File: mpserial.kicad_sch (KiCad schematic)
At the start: 12 parts, among them J1 USB_A, Q1 Q_Photo_NPN, U1 FT230XS, U2 ${SIM.PARAMS}

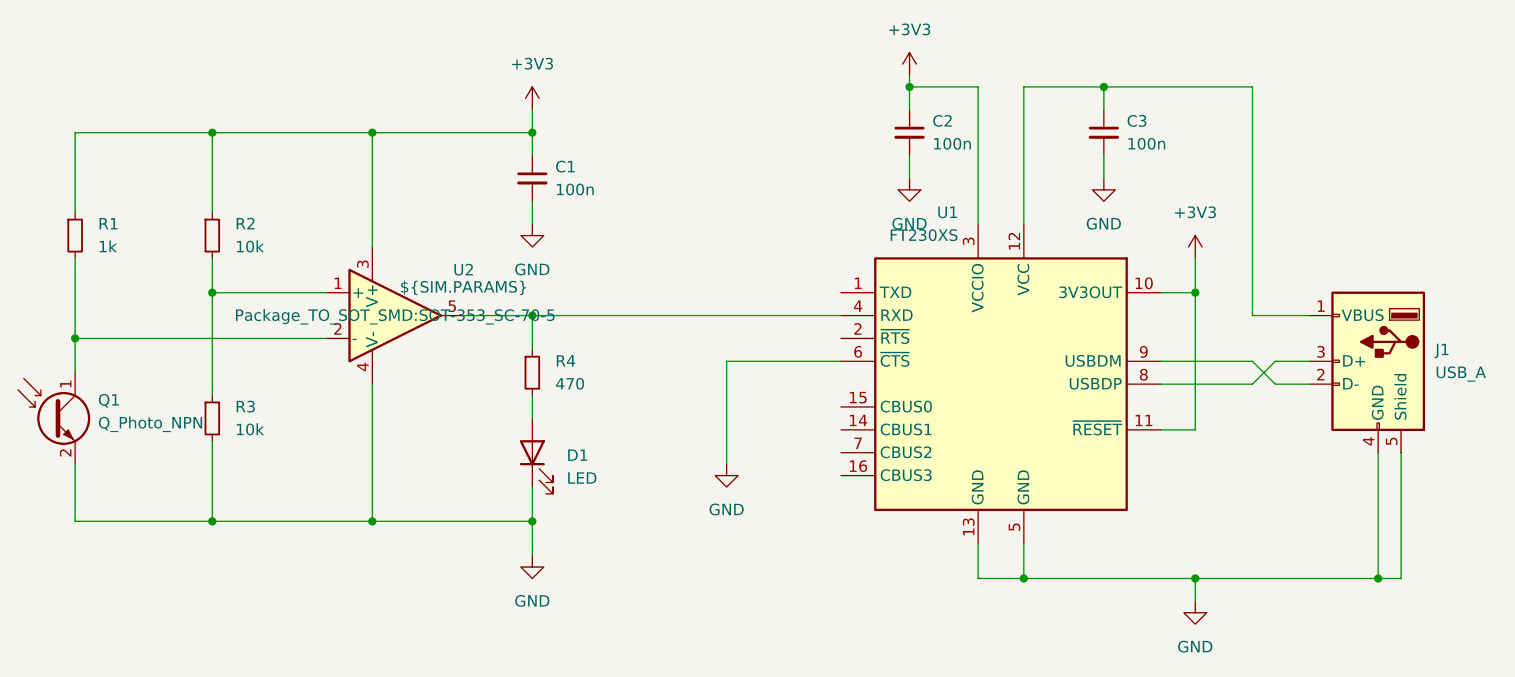
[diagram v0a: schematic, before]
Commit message: corrected opamp footprint and symbol names, changed USB-A connector to throughhole for cheaper assembly
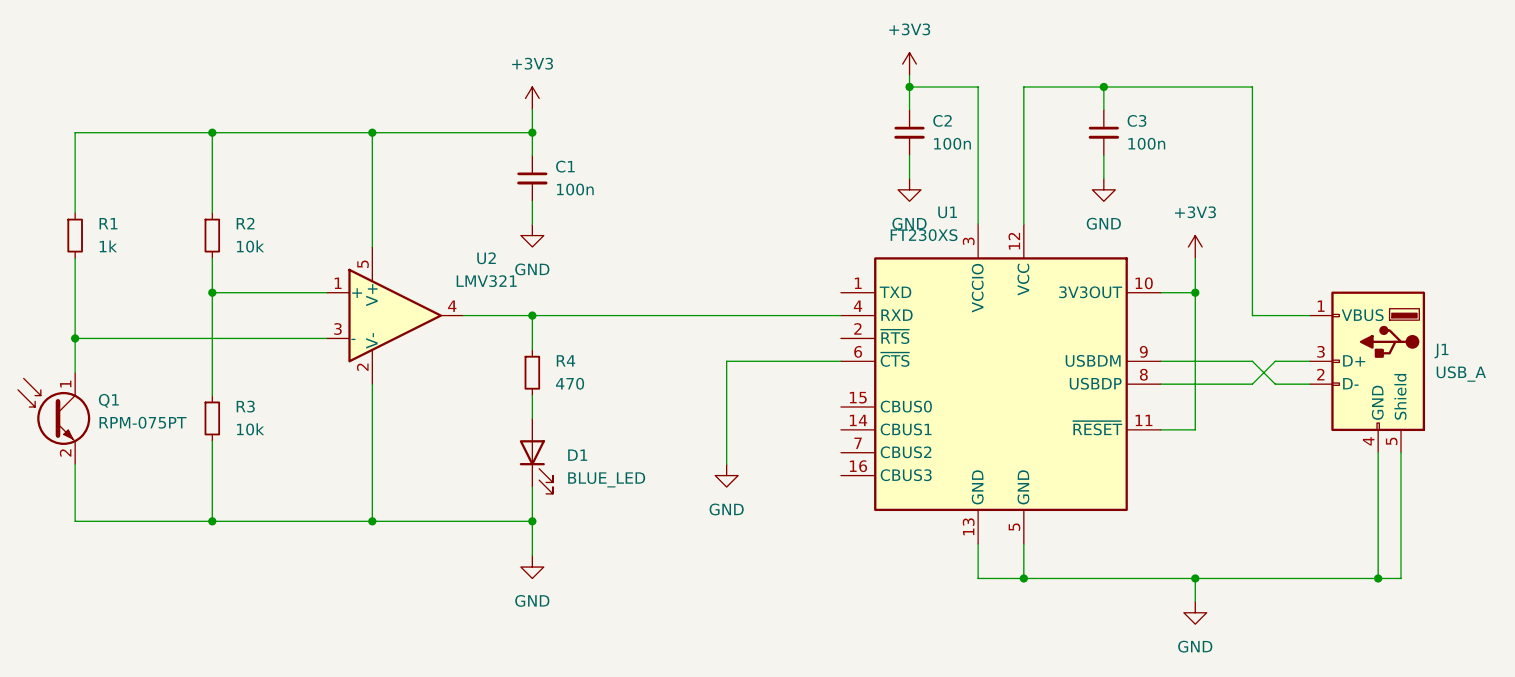
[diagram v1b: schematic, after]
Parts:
- removed U2: ${SIM.PARAMS}, Package_TO_SOT_SMD:SOT-353_SC-70-5, symbol Simulation_SPICE:OPAMP
- added U2: LMV321, Package_TO_SOT_SMD:SOT-353_SC-70-5, symbol Amplifier_Operational:LMV321
- D1: value LED -> BLUE_LED
- J1: footprint Connector_USB:USB_A_Molex_48037-2200_Horizontal -> My Footprints:CONN_USB_A_MALE_HORIZONTAL_TH
- Q1: value Q_Photo_NPN -> RPM-075PT
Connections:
- net +3V3: now also U2.5 (V+)
- net GND: now also U2.2 (V-)
- net at R4.1, U1.4 (RXD): now also U2.4
- net at R2.2, R3.1: now also U2.1 (+)
- net at Q1.1 (C), R1.2: now also U2.3 (-)
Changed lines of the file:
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@@
-	)
-	(symbol
-		(lib_id "Simulation_SPICE:OPAMP")
-		(at 74.93 87.63 0)
-		(unit 1)
-		(exclude_from_sim no)
-		(in_bom yes)
-		(on_board yes)
-		(dnp no)
-		(fields_autoplaced yes)
-		(property "Reference" "U2"
-			(at 82.55 82.5814 0)
-			(effects
-				(font
-					(size 1.27 1.27)
-				)
-			)
-		)
-		(property "Value" "${SIM.PARAMS}"
-			(at 82.55 84.4865 0)
-			(effects
-				(font
-					(size 1.27 1.27)
-				)
-			)
-		)
-		(property "Footprint" "Package_TO_SOT_SMD:SOT-353_SC-70-5"
-			(at 74.93 87.63 0)
-			(effects
-				(font
-					(size 1.27 1.27)
-				)
-			)
-		)
-		(property "Datasheet" "https://ngspice.sourceforge.io/docs/ngspice-html-manual/manual.xhtml#sec__SUBCKT_Subcircuits"
-			(at 74.93 87.63 0)
-			(effects
-				(font
-					(size 1.27 1.27)
-				)
-				(hide yes)
-			)
-		)
-		(property "Description" "Operational amplifier, single, node sequence=1:+ 2:- 3:OUT 4:V+ 5:V-"
-			(at 74.93 87.63 0)
-			(effects
-				(font
-					(size 1.27 1.27)
-				)
-				(hide yes)
-			)
-		)
-		(property "Sim.Pins" "1=in+ 2=in- 3=vcc 4=vee 5=out"
-			(at 74.93 87.63 0)
-			(effects
-				(font
-					(size 1.27 1.27)
-				)
-				(hide yes)
-			)
-		)
-		(property "Sim.Device" "SUBCKT"
-			(at 74.93 87.63 0)
-			(effects
-				(font
-					(size 1.27 1.27)
-				)
-				(justify left)
-				(hide yes)
-			)
-		)
-		(property "Sim.Library" "${KICAD8_SYMBOL_DIR}/Simulation_SPICE.sp"
-			(at 74.93 87.63 0)
-			(effects
-				(font
-					(size 1.27 1.27)
-				)
-				(hide yes)
-			)
-		)
-		(property "Sim.Name" "kicad_builtin_opamp"
-			(at 74.93 87.63 0)
-			(effects
-				(font
-					(size 1.27 1.27)
-				)
-				(hide yes)
-			)
-		)
-		(pin "1"
-		)
-		(pin "3"
-		)
-		(pin "5"
-		)
-		(pin "4"
-		)
-		(pin "2"
-		)
-		(instances
-			(project ""
-				(path "/7ebcebd8-6e74-48ea-a3c7-a4b7113dc1a4"
-					(reference "U2")
-					(unit 1)
-				)
-			)
-		)
 	)
 	(symbol
@@
 			)
 		)
-		(property "Footprint" "Connector_USB:USB_A_Molex_48037-2200_Horizontal"
+		(property "Footprint" "My Footprints:CONN_USB_A_MALE_HORIZONTAL_TH"
 			(at 180.34 93.98 0)
 			(effects
@@
 	)
 	(symbol
+		(lib_id "Amplifier_Operational:LMV321")
+		(at 74.93 87.63 0)
+		(unit 1)
+		(exclude_from_sim no)
+		(in_bom yes)
+		(on_board yes)
+		(dnp no)
+		(fields_autoplaced yes)
+		(property "Reference" "U2"
+			(at 85.09 81.3114 0)
+			(effects
+				(font
+					(size 1.27 1.27)
+				)
+			)
+		)
+		(property "Value" "LMV321"
+			(at 85.09 83.8514 0)
+			(effects
+				(font
+					(size 1.27 1.27)
+				)
+			)
+		)
+		(property "Footprint" "Package_TO_SOT_SMD:SOT-353_SC-70-5"
+			(at 74.93 87.63 0)
+			(effects
+				(font
+					(size 1.27 1.27)
+				)
+				(justify left)
+				(hide yes)
+			)
+		)
+		(property "Datasheet" "http://www.ti.com/lit/ds/symlink/lmv324.pdf"
+			(at 74.93 87.63 0)
+			(effects
+				(font
+					(size 1.27 1.27)
+				)
+				(hide yes)
+			)
+		)
+		(property "Description" "Low-Voltage Rail-to-Rail Output Operational Amplifiers, SOT-23-5/SC-70-5"
+			(at 74.93 87.63 0)
+			(effects
+				(font
+					(size 1.27 1.27)
+				)
+				(hide yes)
+			)
+		)
+		(pin "2"
+		)
+		(pin "4"
+		)
+		(pin "3"
+		)
+		(pin "5"
+		)
+		(pin "1"
+		)
+		(instances
+			(project ""
+				(path "/7ebcebd8-6e74-48ea-a3c7-a4b7113dc1a4"
+					(reference "U2")
+					(unit 1)
+				)
+			)
+		)
+	)
+	(symbol
 		(lib_id "Device:C_Small")
 		(at 132.08 67.31 0)
@@
 			)
 		)
-		(property "Value" "Q_Photo_NPN"
+		(property "Value" "RPM-075PT"
 			(at 41.91 99.5806 0)
 			(effects
@@
 			)
 		)
-		(property "Value" "LED"
+		(property "Value" "BLUE_LED"
 			(at 93.98 105.7274 90)
 			(effects
